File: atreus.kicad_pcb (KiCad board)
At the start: 2 copper layers, 232 x 90 mm, 98 parts, among them U1 ATmega32U4-AU, Y1 Crystal_GND24_Small

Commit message: fuse.
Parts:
- added 500mA: F1, Fuse_Holders_and_Fuses:Fuse_SMD1206_Reflow, F.Cu at (143.0, 45.0)
- moved R3 3.00 mm to (140.0, 45.0)
- moved R2 2.00 mm to (138.0, 45.0)
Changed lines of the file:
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@@
    (layers *.Cu *.Mask)))
 (module Resistors_SMD:R_0805 (layer F.Cu)
-  (at 140 45 90)
+  (at 138 45 90)
   (descr "Resistor SMD 0805, reflow soldering, Vishay (see dcrcw.pdf)")
   (tags "resistor 0805")
@@
    (net 68 D+)))
 (module Resistors_SMD:R_0805 (layer F.Cu)
-  (at 143 45 90)
+  (at 140 45 90)
   (descr "Resistor SMD 0805, reflow soldering, Vishay (see dcrcw.pdf)")
   (tags "resistor 0805")
@@
    (layers F.Cu F.Paste F.Mask)
    (net 67 D-)))
+(module Fuse_Holders_and_Fuses:Fuse_SMD1206_Reflow (layer F.Cu)
+  (at 143 45 270)
+  (descr "Fuse, Sicherung, SMD1206, Littlefuse-Wickmann, Reflow,")
+  (tags "Fuse Sicherung SMD1206 Littlefuse-Wickmann Reflow ")
+  (attr smd)
+  (attr smd)
+  (fp_text
+   reference
+   500mA
+   (at -0.1 -2.75 270)
+   (layer F.SilkS)
+   (effects (font (size 1 1) (thickness 0.15))))
+  (fp_text
+   value
+   F1
+   (at -0.45 3.2 270)
+   (layer F.Fab)
+   (effects (font (size 1 1) (thickness 0.15))))
+  (fp_line (start 2.47 1.05) (end -2.47 1.05) (layer F.CrtYd) (width 0.05))
+  (fp_line (start 2.47 1.05) (end 2.47 -1.05) (layer F.CrtYd) (width 0.05))
+  (fp_line (start -2.47 -1.05) (end -2.47 1.05) (layer F.CrtYd) (width 0.05))
+  (fp_line (start -2.47 -1.05) (end 2.47 -1.05) (layer F.CrtYd) (width 0.05))
+  (fp_line (start -1 -1.07) (end 1 -1.07) (layer F.SilkS) (width 0.12))
+  (fp_line (start 1 1.07) (end -1 1.07) (layer F.SilkS) (width 0.12))
+  (fp_line (start -1.6 -0.8) (end 1.6 -0.8) (layer F.Fab) (width 0.1))
+  (fp_line (start 1.6 -0.8) (end 1.6 0.8) (layer F.Fab) (width 0.1))
+  (fp_line (start 1.6 0.8) (end -1.6 0.8) (layer F.Fab) (width 0.1))
+  (fp_line (start -1.6 0.8) (end -1.6 -0.8) (layer F.Fab) (width 0.1))
+  (pad
+   1
+   smd
+   rect
+   (at -1.2 0)
+   (size 2.03 1.14)
+   (layers F.Cu F.Paste F.Mask)
+   (net 63 VCC))
+  (pad
+   2
+   smd
+   rect
+   (at 1.2 0)
+   (size 2.03 1.14)
+   (layers F.Cu F.Paste F.Mask)
+   (net 102 +5V)))
 (gr_line (start 31 22) (end 84 22) (angle 90) (layer Edge.Cuts) (width 0.3))
 (gr_line (start 84 22) (end 127 30) (angle 90) (layer Edge.Cuts) (width 0.3))

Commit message: autorouting
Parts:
- removed the D2:2 at (46.3, 31.2)
- removed the D2:2 at (81.8, 48.6)
- removed the D2:2 at (78.5, 67.3)
- removed the D2:2 at (75.2, 86.0)
- removed the D2:2 at (102.8, 39.1)
- removed the D2:2 at (99.5, 57.8)
- removed the D2:2 at (96.2, 76.5)
- removed the D2:2 at (92.9, 95.2)
- removed the D2:2 at (120.6, 47.3)
- removed the D2:2 at (117.3, 66.0)
- removed the D2:2 at (114.0, 84.8)
- removed the D2:2 at (43.0, 49.9)
- removed the D2:2 at (110.7, 103.5)
- removed the D2:2 at (130.0, 103.8)
- removed the D2:2 at (138.3, 103.8)
- removed the D2:2 at (147.6, 47.3)
- removed the D2:2 at (150.9, 66.0)
- removed the D2:2 at (154.2, 84.7)
- removed the D2:2 at (157.5, 103.5)
- removed the D2:2 at (165.4, 39.1)
- removed the D2:2 at (168.7, 57.8)
- removed the D2:2 at (172.0, 76.5)
- removed the D2:2 at (39.7, 68.6)
- removed the D2:2 at (175.3, 95.2)
- removed the D2:2 at (183.1, 29.9)
- removed the D2:2 at (186.4, 48.6)
- removed the D2:2 at (189.7, 67.3)
- removed the D2:2 at (193.0, 86.0)
- removed the D2:2 at (202.7, 31.5)
- removed the D2:2 at (206.0, 50.2)
- removed the D2:2 at (209.3, 68.9)
- removed the D2:2 at (212.6, 87.7)
- removed the D2:2 at (221.9, 31.2)
- removed the D2:2 at (36.4, 87.3)
- removed the D2:2 at (225.2, 49.9)
- removed the D2:2 at (228.5, 68.6)
- removed the D2:2 at (231.8, 87.3)
- removed the D2:2 at (65.6, 31.5)
- removed the D2:2 at (62.3, 50.2)
- removed the D2:2 at (59.0, 68.9)
- removed the D2:2 at (55.7, 87.7)
- removed the D2:2 at (85.1, 29.9)
- added D0:0: , DIODE, F.Cu at (46.3, 31.2)
- added D0:1: , DIODE, F.Cu at (43.0, 49.9)
- added D0:2: , DIODE, F.Cu at (39.7, 68.6)
- added D0:3: , DIODE, F.Cu at (36.4, 87.3)
- added D10:0: , DIODE, F.Cu at (202.7, 31.5)
- added D10:1: , DIODE, F.Cu at (206.0, 50.2)
- added D10:2: , DIODE, F.Cu at (209.3, 68.9)
- added D10:3: , DIODE, F.Cu at (212.6, 87.7)
- added D11:0: , DIODE, F.Cu at (221.9, 31.2)
- added D11:1: , DIODE, F.Cu at (225.2, 49.9)
- added D11:2: , DIODE, F.Cu at (228.5, 68.6)
- added D11:3: , DIODE, F.Cu at (231.8, 87.3)
- added D1:0: , DIODE, F.Cu at (65.6, 31.5)
- added D1:1: , DIODE, F.Cu at (62.3, 50.2)
- added D1:2: , DIODE, F.Cu at (59.0, 68.9)
- added D1:3: , DIODE, F.Cu at (55.7, 87.7)
- added D2:0: , DIODE, F.Cu at (85.1, 29.9)
- added D2:1: , DIODE, F.Cu at (81.8, 48.6)
- added D2:2: , DIODE, F.Cu at (78.5, 67.3)
- added D2:3: , DIODE, F.Cu at (75.2, 86.0)
- added D3:0: , DIODE, F.Cu at (102.8, 39.1)
- added D3:1: , DIODE, F.Cu at (99.5, 57.8)
- added D3:2: , DIODE, F.Cu at (96.2, 76.5)
- added D3:3: , DIODE, F.Cu at (92.9, 95.2)
- added D4:0: , DIODE, F.Cu at (120.6, 47.3)
- added D4:1: , DIODE, F.Cu at (117.3, 66.0)
- added D4:2: , DIODE, F.Cu at (114.0, 84.8)
- added D4:3: , DIODE, F.Cu at (110.7, 103.5)
- added D5:0: , DIODE, F.Cu at (130.0, 103.8)
- added D6:0: , DIODE, F.Cu at (138.3, 103.8)
- added D7:0: , DIODE, F.Cu at (147.6, 47.3)
- added D7:1: , DIODE, F.Cu at (150.9, 66.0)
- added D7:2: , DIODE, F.Cu at (154.2, 84.7)
- added D7:3: , DIODE, F.Cu at (157.5, 103.5)
- added D8:0: , DIODE, F.Cu at (165.4, 39.1)
- added D8:1: , DIODE, F.Cu at (168.7, 57.8)
- added D8:2: , DIODE, F.Cu at (172.0, 76.5)
- added D8:3: , DIODE, F.Cu at (175.3, 95.2)
- added D9:0: , DIODE, F.Cu at (183.1, 29.9)
- added D9:1: , DIODE, F.Cu at (186.4, 48.6)
- added D9:2: , DIODE, F.Cu at (189.7, 67.3)
- added D9:3: , DIODE, F.Cu at (193.0, 86.0)
- REF**: value Molex-0548190589 -> (none)
- moved C1 45.0 mm to (135.0, 90.0)
- moved C2 45.0 mm to (125.0, 90.0)
- moved Y1 45.0 mm to (130.0, 90.0)
- moved R2 21.9 mm to (122.0, 60.0)
- moved R3 21.2 mm to (125.0, 60.0)
- moved 500mA 5.83 mm to (140.0, 50.0)
- moved C6 5.00 mm to (140.0, 65.0)
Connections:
- U1 pad 1: N-col-5 -> N-col-0
- U1 pad 10: N-row-2 -> N-col-2
- U1 pad 11: N-col-9 -> N-col-3
- U1 pad 12: Net-U1-Pad12 -> N-col-4
- U1 pad 18: N-col-3 -> N-row-2
- U1 pad 19: N-col-2 -> N-row-3
- U1 pad 25: N-col-4 -> N-col-5
- U1 pad 26: Net-U1-Pad26 -> N-col-7
- U1 pad 27: N-col-1 -> N-col-8
- U1 pad 28: N-row-0 -> N-col-9
- U1 pad 29: N-row-1 -> N-col-10
- U1 pad 30: N-row-3 -> (no net)
- U1 pad 31: N-col-0 -> N-col-6
- U1 pad 36: N-col-6 -> (no net)
- U1 pad 37: N-col-7 -> N-row-0
- U1 pad 38: N-col-8 -> N-row-1
- U1 pad 9: N-col-10 -> N-col-1
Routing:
- net N-row-3: track 0.00 -> 349.8 mm, vias 0 -> 2
- net N-row-2: track 0.00 -> 332.7 mm, vias 0 -> 2
- net N-row-0: track 2.02 -> 288.8 mm, vias 0 -> 1
- net N-row-1: track 0.00 -> 272.9 mm, vias 0 -> 1
- net N-col-10: track 0.00 -> 187.1 mm, vias 0 -> 2
- net N-col-0: track 0.00 -> 171.8 mm
- net N-col-9: track 0.00 -> 157.7 mm
- net N-col-1: track 0.00 -> 156.7 mm
- net N-col-2: track 0.00 -> 143.2 mm
- net GND: track 0.00 -> 143.0 mm, vias 0 -> 6
- net N-col-8: track 0.00 -> 137.4 mm, vias 0 -> 2
- net N-col-3: track 0.00 -> 118.3 mm, vias 0 -> 1
- net N-col-7: track 0.00 -> 116.7 mm
- net N-col-6: track 0.00 -> 99.3 mm, vias 0 -> 1
- net N-col-4: track 0.00 -> 98.4 mm, vias 0 -> 1
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
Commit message: manually traced the thing.
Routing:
- net GND: track 143.0 -> 0.00 mm, vias 6 -> 0
- net 59: track 0.00 -> 131.0 mm, vias 0 -> 6
- net +5V: track 89.8 -> 0.00 mm
- net 62: track 0.00 -> 86.7 mm
- net N-row-3: track 349.8 -> 265.4 mm, vias 2 -> 0
- net N-row-2: track 332.7 -> 272.8 mm, vias 2 -> 0
- net N-row-0: track 288.8 -> 230.0 mm
- net N-row-1: track 272.9 -> 229.3 mm
- net 66: track 0.00 -> 32.0 mm, vias 0 -> 2
- net Net-C2-Pad1: track 24.8 -> 0.00 mm
- net D+: track 33.5 -> 15.1 mm, vias 0 -> 2
- net Net-R2-Pad1: track 17.7 -> 0.00 mm, vias 2 -> 0
- net 65: track 0.00 -> 17.2 mm, vias 0 -> 2
- net 58: track 0.00 -> 17.2 mm
- net 60: track 0.00 -> 16.0 mm, vias 0 -> 2
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
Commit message: hand routing, again.
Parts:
- moved C4 5.00 mm to (123.0, 90.0), turned to 135 degrees
- moved C2 4.50 mm to (129.5, 90.0), turned to 135 degrees
- moved R1 4.00 mm to (123.0, 84.0), turned to 0 degrees
- moved Y1 3.91 mm to (132.5, 87.0), turned to 225 degrees
- moved C1 0.50 mm to (135.5, 90.0), turned to 45 degrees
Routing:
- net 58: track 17.2 -> 11.0 mm
- net 60: track 16.0 -> 10.5 mm, vias 2 -> 0
- net 62: track 86.7 -> 89.4 mm
- net 64: track 9.54 -> 8.31 mm
- net N-row-2: track 272.8 -> 271.8 mm
- net 59: track 131.0 -> 130.2 mm, vias 6 -> 7

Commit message: hand routing, again. again.
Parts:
- moved C7 22.1 mm to (145.0, 72.0)
- moved C4 18.1 mm to (125.0, 72.0), turned to 90 degrees
- moved R1 17.3 mm to (126.0, 67.0)
- moved C3 17.0 mm to (133.0, 64.0)
- moved C5 16.6 mm to (131.0, 84.0), turned to 0 degrees
- moved C6 15.8 mm to (145.0, 80.0), turned to 270 degrees
- moved C2 15.3 mm to (120.0, 78.0), turned to 90 degrees
- moved R4 14.9 mm to (140.0, 84.0), turned to 180 degrees
- moved C1 14.0 mm to (124.0, 82.0), turned to 0 degrees
- moved Y1 12.4 mm to (124.0, 78.0), turned to 180 degrees
- moved R2 12.1 mm to (133.0, 55.0)
- moved R3 12.1 mm to (136.0, 55.0)
- moved 500mA 5.00 mm to (140.0, 55.0)
- moved U1 1.50 mm to (135.0, 75.0), turned to 270 degrees
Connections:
- U1 pad 1: N-col-0 -> (no net)
- U1 pad 10: N-col-2 -> N-col-3
- U1 pad 11: N-col-3 -> N-col-4
- U1 pad 12: N-col-4 -> (no net)
- U1 pad 18: N-row-2 -> (no net)
- U1 pad 19: N-row-3 -> (no net)
- U1 pad 22: Net-U1-Pad22 -> N-col-5
- U1 pad 25: N-col-5 -> N-col-0
- U1 pad 26: N-col-7 -> N-col-1
- U1 pad 27: N-col-8 -> N-col-6
- U1 pad 28: N-col-9 -> N-col-7
- U1 pad 29: N-col-10 -> N-col-8
- U1 pad 30: (no net) -> N-col-9
- U1 pad 31: N-col-6 -> N-col-10
- U1 pad 36: (no net) -> N-row-3
- U1 pad 37: N-row-0 -> N-row-2
- U1 pad 39: Net-U1-Pad39 -> N-row-0
- U1 pad 9: N-col-1 -> N-col-2
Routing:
- net N-col-1: track 150.7 -> 177.9 mm
- net N-col-0: track 172.0 -> 195.6 mm
- net N-col-9: track 165.1 -> 184.9 mm
- net N-col-8: track 143.7 -> 162.9 mm
- net N-col-10: track 181.8 -> 200.9 mm
- net N-col-7: track 125.3 -> 143.7 mm
- net N-col-6: track 110.8 -> 126.5 mm, vias 2 -> 1
- net N-col-2: track 128.5 -> 143.0 mm
- net N-row-2: track 271.8 -> 257.6 mm
- net 62: track 89.4 -> 75.3 mm
- net 66: track 32.0 -> 18.0 mm, vias 2 -> 0
- net D-: track 30.3 -> 18.0 mm, vias 2 -> 0
- net 59: track 130.2 -> 118.8 mm, vias 7 -> 4
- net N-row-1: track 229.3 -> 220.6 mm, vias 1 -> 0
- net N-col-5: track 84.6 -> 76.1 mm, vias 2 -> 0
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
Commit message: cosmetics.
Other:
- board text added: "Just Do It!"
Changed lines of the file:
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@@
       (outputdirectory "atrgbr/"))
   )
-  (gr_text AtreuSMD (at 134 93) (layer F.SilkS)
+  (gr_text AtreuSMD (at 134 47) (layer F.SilkS)
     (effects (font (size 4 3) (thickness 0.3048)))
   )
+  (gr_text "Just Do It!" (at 134 92.5) (layer F.SilkS)
+    (effects (font (size 2.032 1.524) (thickness 0.3048)))
+  )
   (gr_text "Phil Hagelberg & Greasy Shit Gang" (at 107 31 350) (layer F.SilkS)
     (effects (font (size 2.032 1.524) (thickness 0.3048)))
@@
    (net 1 N-row-0)))
 (module Keebio-Parts:MX-Alps-Choc-1U-NoLED (layer Front)
-  (at 90.50418478725454 57.81745532799191 -10)
+  (at 90.50418478725455 57.81745532799191 -10)
   (fp_text
    reference
@@
    (net 8 N-col-3)))
 (module DIODE (layer Front)
-  (at 99.50418478725454 57.81745532799191 80)
+  (at 99.50418478725455 57.81745532799191 80)
   (attr smd)
   (fp_text
@@
    (net 2 N-row-1)))
 (module Keebio-Parts:MX-Alps-Choc-1U-NoLED (layer Front)
-  (at 237.52398385946222 68.59437213050145 10)
+  (at 237.52398385946222 68.59437213050146 10)
   (fp_text
    reference
@@
    (net 42 N-diode-26)))
 (module DIODE (layer Front)
-  (at 228.52398385946222 68.59437213050145 100)
+  (at 228.52398385946222 68.59437213050146 100)
   (attr smd)
   (fp_text

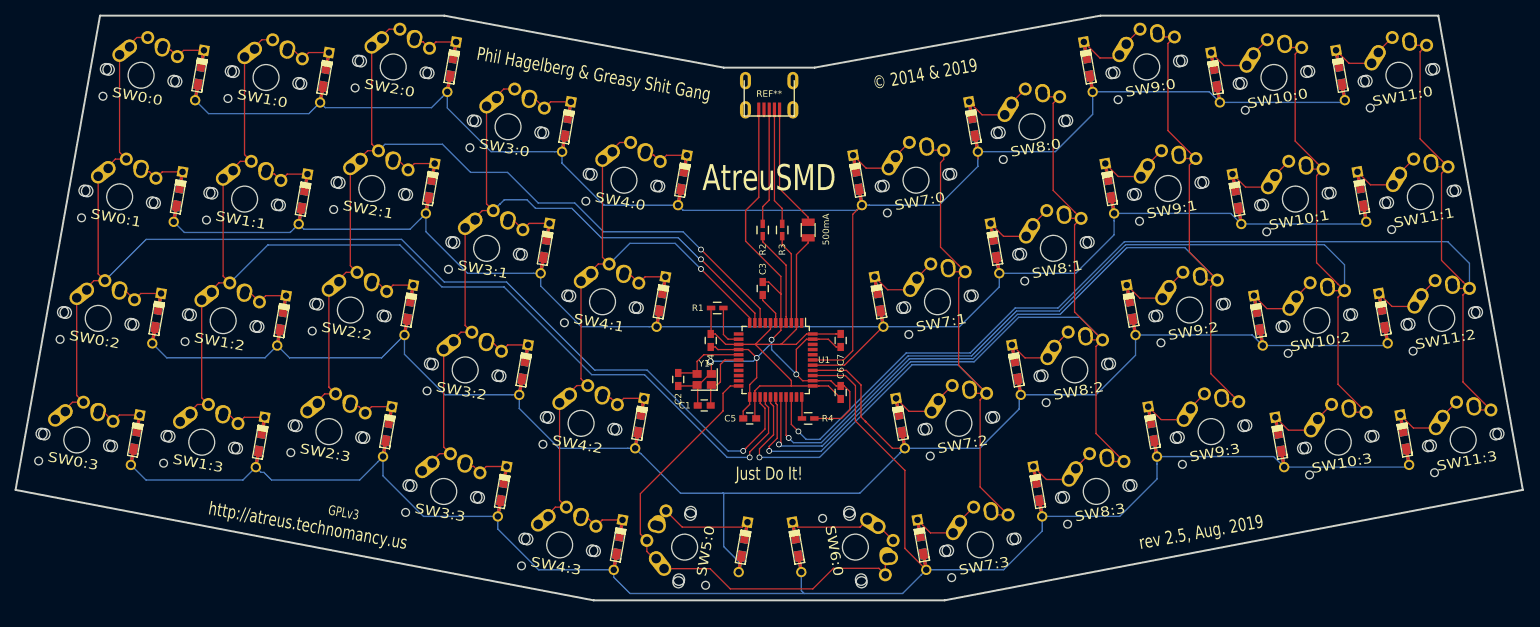
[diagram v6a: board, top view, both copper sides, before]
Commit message: 44 keys.
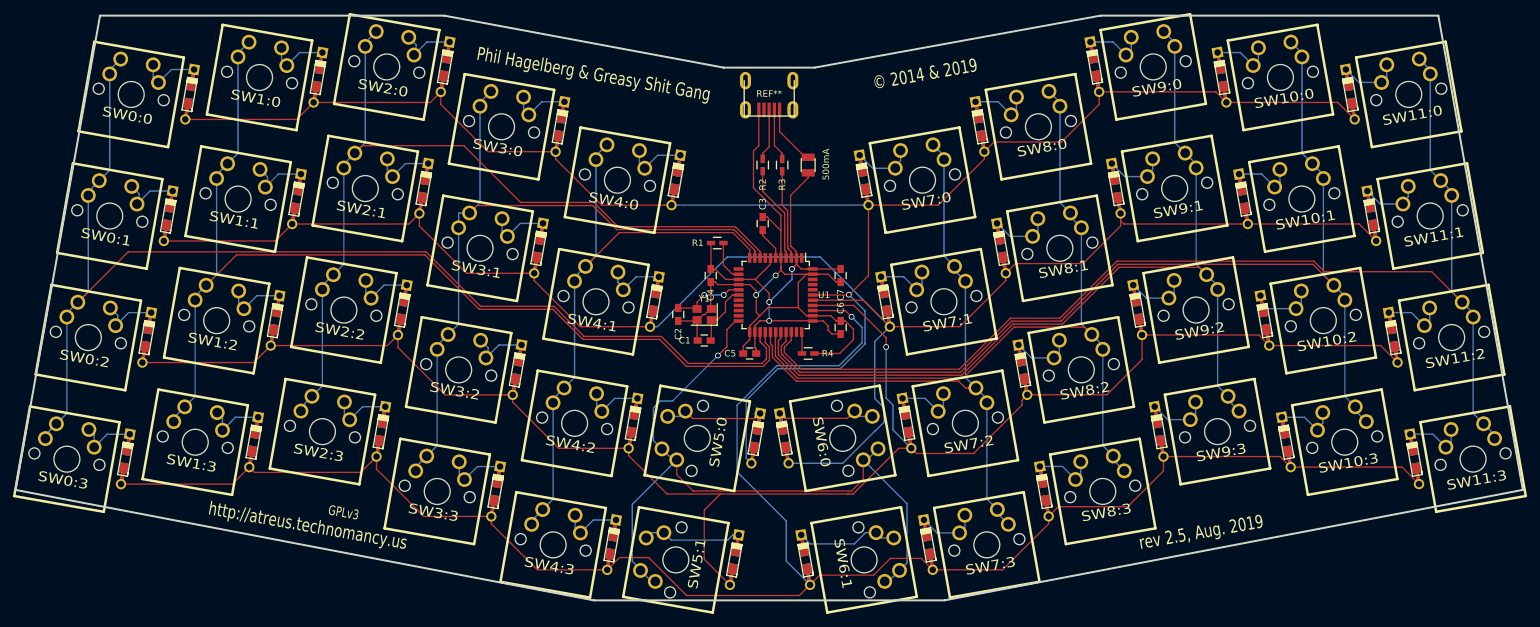
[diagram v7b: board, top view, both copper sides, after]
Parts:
- added D5:1: , DIODE, F.Cu at (128.6, 105.8)
- added D6:1: , DIODE, F.Cu at (139.6, 105.8)
- added SW5:1: , Keebio-Parts:MX-Alps-Choc-1U-NoLED, F.Cu at (119.6, 105.8)
- added SW6:1: , Keebio-Parts:MX-Alps-Choc-1U-NoLED, F.Cu at (148.6, 105.8)
- moved D5:0 16.9 mm to (131.9, 87.1)
- moved SW5:0 16.9 mm to (122.9, 87.1)
- moved D6:0 16.9 mm to (136.3, 87.1)
- moved SW6:0 16.9 mm to (145.3, 87.1)
- moved 500mA 10.0 mm to (140.0, 45.0)
- moved C1 10.0 mm to (124.0, 72.0)
- moved C2 10.0 mm to (120.0, 68.0)
- moved C3 10.0 mm to (133.0, 54.0)
- moved C4 10.0 mm to (125.0, 62.0)
- moved C5 10.0 mm to (131.0, 74.0)
- moved C6 10.0 mm to (145.0, 70.0)
- moved C7 10.0 mm to (145.0, 62.0)
- moved R1 10.0 mm to (126.0, 57.0)
- moved R2 10.0 mm to (133.0, 45.0)
- moved R3 10.0 mm to (136.0, 45.0)
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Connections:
- net N-diode-21 renamed N-diode-42
- net N-diode-22 renamed N-diode-43
- net N-diode-23 renamed N-diode-44
- net N-diode-25 renamed N-diode-45
- net N-diode-26 renamed N-diode-46
- net N-diode-27 renamed N-diode-47
- D5:0 pad 2: N-row-2 -> N-row-0
- D6:0 pad 2: N-row-3 -> N-row-1
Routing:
- net 59: track 118.8 -> 0.00 mm, vias 4 -> 0
- net GND: track 0.00 -> 109.1 mm, vias 0 -> 2
- net 62: track 75.3 -> 0.00 mm
- net +5V: track 0.00 -> 73.3 mm, vias 0 -> 3
- net N-row-1: track 220.6 -> 263.7 mm
- net N-col-5: track 76.1 -> 115.4 mm, vias 0 -> 1
- net N-row-0: track 233.1 -> 262.7 mm, vias 0 -> 1
- net N-col-6: track 126.5 -> 100.5 mm, vias 1 -> 0
- net N-row-3: track 269.6 -> 295.0 mm, vias 0 -> 1
- net N-col-9: track 184.9 -> 161.3 mm, vias 1 -> 0
- net N-col-7: track 143.7 -> 120.8 mm, vias 1 -> 0
- net N-col-8: track 162.9 -> 141.5 mm, vias 1 -> 0
- net N-col-10: track 200.9 -> 181.7 mm, vias 1 -> 0
- net 66: track 18.0 -> 0.00 mm
- net N-diode-25: track 0.00 -> 15.9 mm
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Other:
- board text removed: "AtreuSMD"
- board text removed: "Just Do It!"

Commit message: added csv.
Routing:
- net GND: track 109.1 -> 0.00 mm, vias 2 -> 0
- net N-diode-45: track 9.37 -> 109.1 mm, vias 0 -> 2
- net 64: track 0.00 -> 73.3 mm, vias 0 -> 3
- net +5V: track 73.3 -> 0.00 mm, vias 3 -> 0
- net N-diode-22: track 0.00 -> 16.4 mm
- net N-diode-23: track 0.00 -> 15.9 mm
- net Net-R2-Pad1: track 14.8 -> 0.00 mm
- net 67: track 0.00 -> 14.8 mm
- net Net-R3-Pad1: track 13.9 -> 0.00 mm
- net 70: track 0.00 -> 13.9 mm
- net Net-C2-Pad1: track 11.2 -> 0.00 mm, vias 2 -> 0
- net Net-C1-Pad1: track 9.87 -> 0.00 mm
- net VCC: track 9.38 -> 0.00 mm
- net 65: track 0.00 -> 9.38 mm
- net N-diode-26: track 0.00 -> 9.37 mm
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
